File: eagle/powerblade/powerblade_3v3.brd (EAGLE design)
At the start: 25.4 x 25.4 mm, 79 parts, among them J1 JTAG_14PIN_IDC-ND, J2 AC_INF45, J4 TC2030-JLINK-NL, Q1 NTS4173, Q4 2SK1829, U1 TPS62122, U2 MCP6V3, U3 MSP430FR5738, U4 NRF51822QF, U6 MAX9910, U7 OPA2369, X1 16MHz, X3 32.768kHz, Y1 UREACH_XTEND

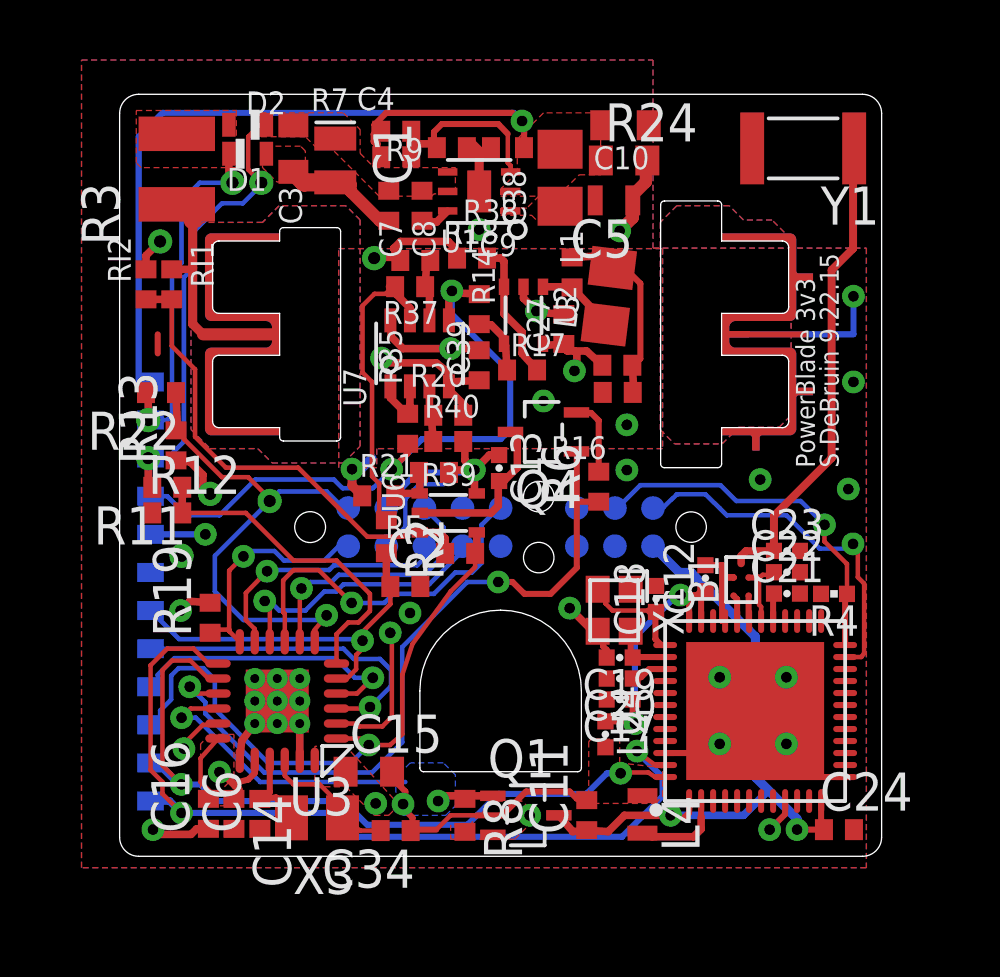
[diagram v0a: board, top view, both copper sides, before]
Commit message: added final v5 part (package) and inputted into powerblade
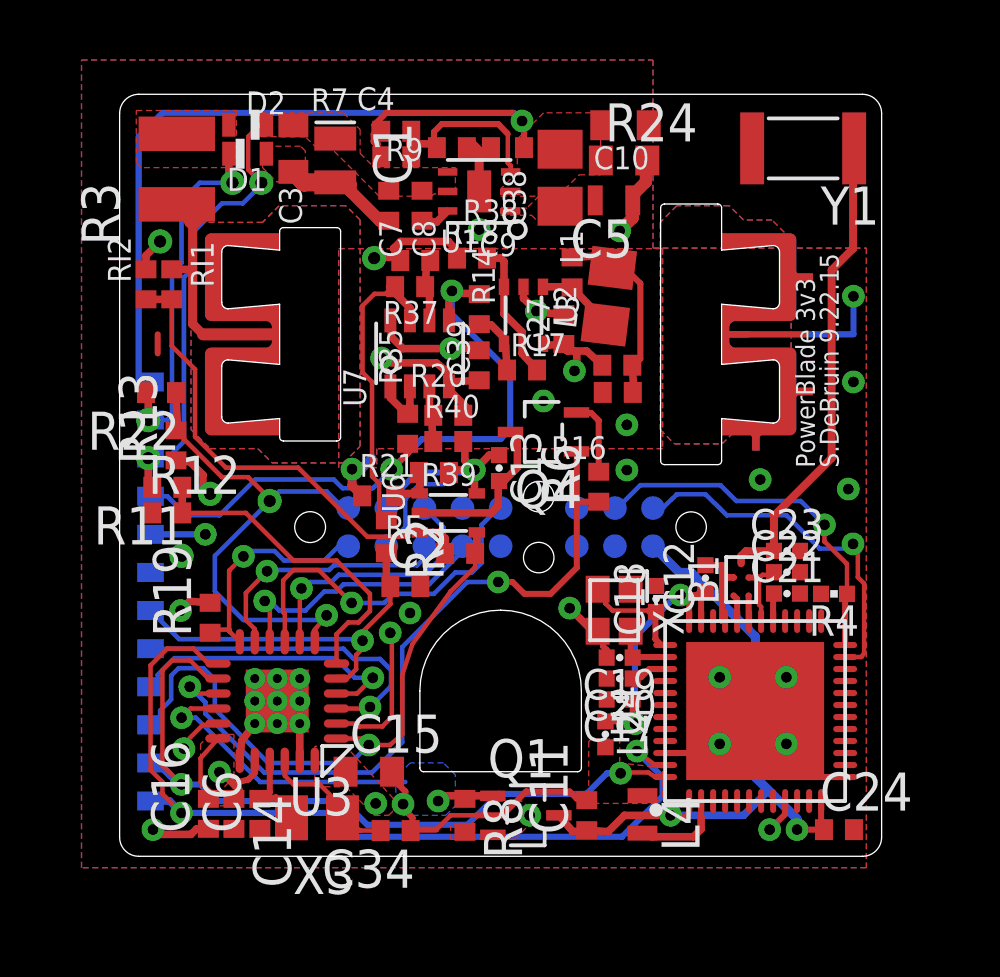
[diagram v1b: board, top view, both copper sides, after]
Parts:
- J2: value AC_INF45 -> AC_INFINAL; device powerfilm:AC3_F45 -> powerfilm:AC3_FINAL
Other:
- outline, holes or cut-outs redrawn
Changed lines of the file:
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@@
 <?xml version="1.0" encoding="utf-8"?>
 <!DOCTYPE eagle SYSTEM "eagle.dtd">
-<eagle version="6.5.0">
+<eagle version="6.3">
 <drawing>
 <settings>
@@
 <attribute name="DIGIKEY" value="490-4025-1-ND" x="4.727575" y="-16.002" size="1.778" layer="27" rot="R270" display="off"/>
 </element>
-<element name="J2" library="powerfilm" package="AC3_F45" value="AC_INF45" x="0" y="0">
+<element name="J2" library="powerfilm" package="AC3_FINAL" value="AC_INFINAL" x="0" y="0">
 <attribute name="DIGIKEY" value="ED1649-ND" x="0" y="0" size="1.778" layer="27" display="off"/>
 <attribute name="DIGIKEY_2" value="ED1649-ND" x="0" y="0" size="1.778" layer="27" display="off"/>
@@
 </signal>
 </signals>
+<errors>
+</errors>
 </board>
 </drawing>
